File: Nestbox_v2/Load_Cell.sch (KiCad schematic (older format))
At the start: 30 parts

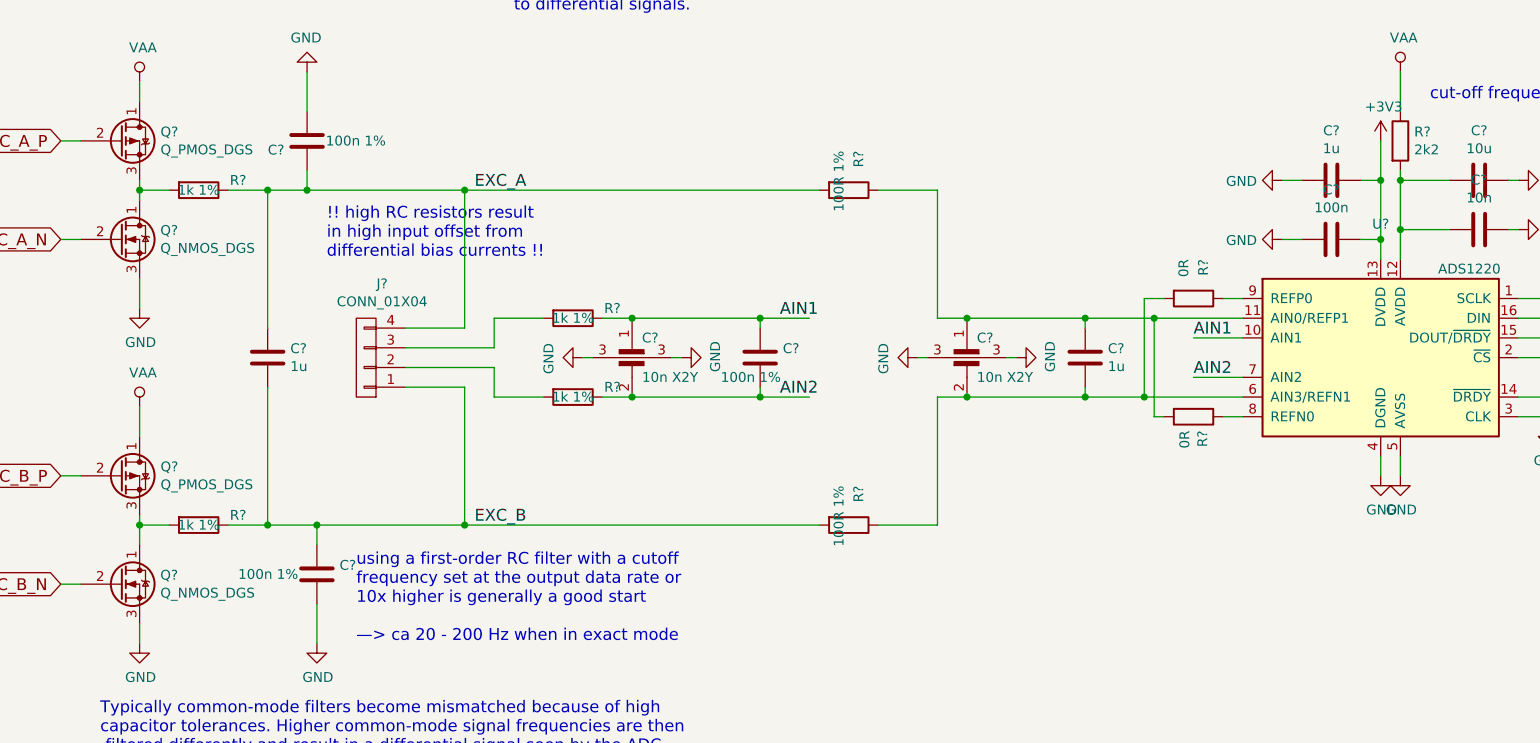
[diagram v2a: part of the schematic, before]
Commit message: created V2 MLX breakout board
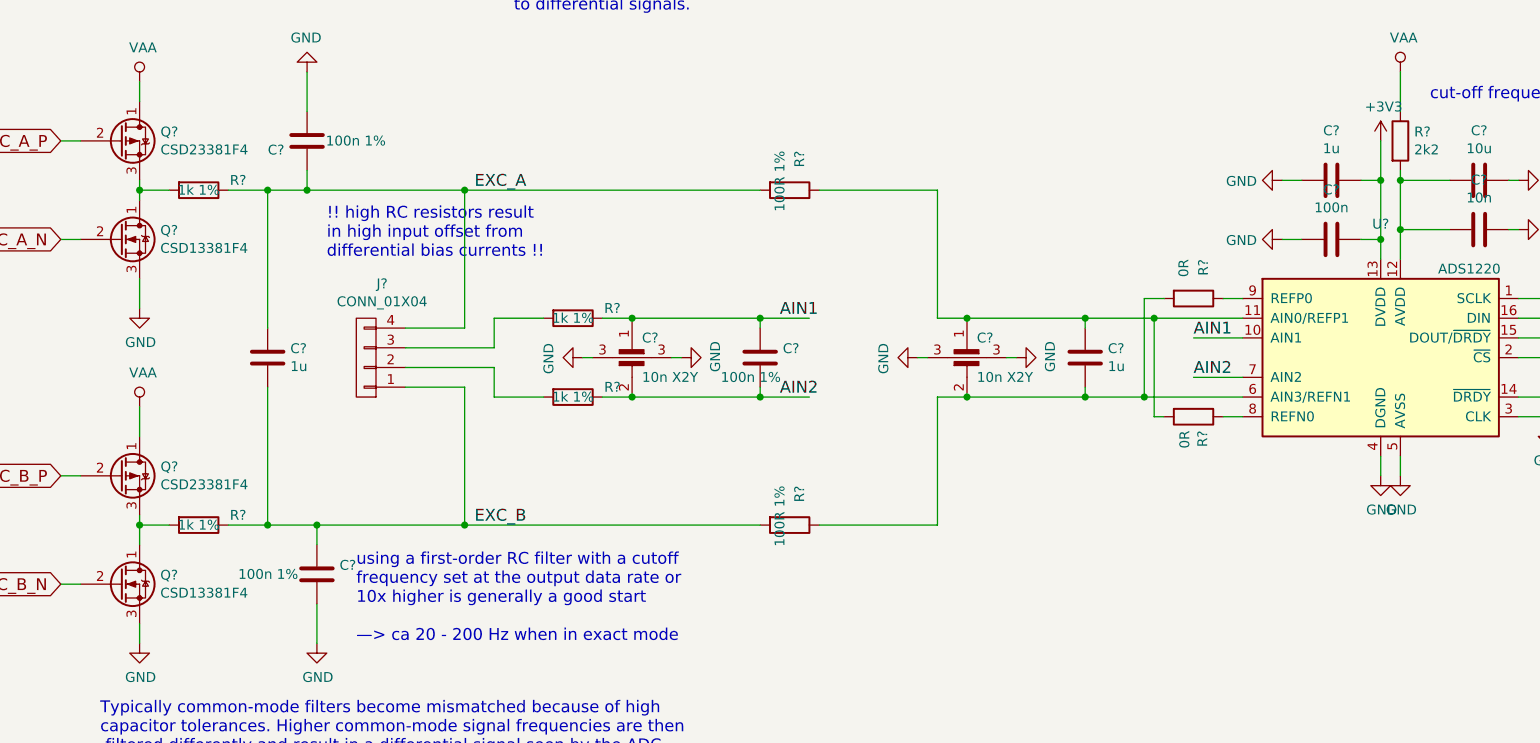
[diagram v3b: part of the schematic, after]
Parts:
- Q? (x2): value Q_NMOS_DGS -> CSD13381F4
- Q? (x2): value Q_PMOS_DGS -> CSD23381F4
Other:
- moved on the sheet: R?
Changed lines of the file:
@@
 P 1550 3400
 F 0 "Q?" H 1755 3446 50  0000 L CNN
-F 1 "Q_NMOS_DGS" H 1755 3355 50  0000 L CNN
+F 1 "CSD13381F4" H 1755 3355 50  0000 L CNN
 F 2 "" H 1750 3500 50  0001 C CNN
 F 3 "" H 1550 3400 50  0001 C CNN
@@
 P 1550 5150
 F 0 "Q?" H 1755 5196 50  0000 L CNN
-F 1 "Q_NMOS_DGS" H 1755 5105 50  0000 L CNN
+F 1 "CSD13381F4" H 1755 5105 50  0000 L CNN
 F 2 "" H 1750 5250 50  0001 C CNN
 F 3 "" H 1550 5150 50  0001 C CNN
@@
 P 1550 4600
 F 0 "Q?" H 1756 4646 50  0000 L CNN
-F 1 "Q_PMOS_DGS" H 1756 4555 50  0000 L CNN
+F 1 "CSD23381F4" H 1756 4555 50  0000 L CNN
 F 2 "" H 1750 4700 50  0001 C CNN
 F 3 "" H 1550 4600 50  0001 C CNN
@@
 P 1550 2900
 F 0 "Q?" H 1756 2946 50  0000 L CNN
-F 1 "Q_PMOS_DGS" H 1756 2855 50  0000 L CNN
+F 1 "CSD23381F4" H 1756 2855 50  0000 L CNN
 F 2 "" H 1750 3000 50  0001 C CNN
 F 3 "" H 1550 2900 50  0001 C CNN
@@
 L R R?
 U 1 1 5AF983FB
-P 5250 3150
-F 0 "R?" H 5050 3200 50  0000 L CNN
-F 1 "100R 1%" H 5050 3100 50  0000 L CNN
-F 2 "" V 5180 3150 50  0001 C CNN
-F 3 "" H 5250 3150 50  0001 C CNN
-	1    5250 3150
+P 4950 3150
+F 0 "R?" H 4750 3200 50  0000 L CNN
+F 1 "100R 1%" H 4750 3100 50  0000 L CNN
+F 2 "" V 4880 3150 50  0001 C CNN
+F 3 "" H 4950 3150 50  0001 C CNN
+	1    4950 3150
 	0    1    1    0
 $EndComp
@@
 L R R?
 U 1 1 5AF9851F
-P 5250 4850
-F 0 "R?" H 5050 4900 50  0000 L CNN
-F 1 "100R 1%" H 5050 4800 50  0000 L CNN
-F 2 "" V 5180 4850 50  0001 C CNN
-F 3 "" H 5250 4850 50  0001 C CNN
-	1    5250 4850
+P 4950 4850
+F 0 "R?" H 4750 4900 50  0000 L CNN
+F 1 "100R 1%" H 4750 4800 50  0000 L CNN
+F 2 "" V 4880 4850 50  0001 C CNN
+F 3 "" H 4950 4850 50  0001 C CNN
+	1    4950 4850
 	0    1    1    0
 $EndComp
@@
 EXC_B_N
 Wire Wire Line
-	8050 3050 8050 3500
+	8050 3050 8050 3100
+Wire Wire Line
+	8050 3100 8050 3350
+Wire Wire Line
+	8050 3350 8050 3500
 Wire Wire Line
 	8050 3100 8300 3100
 Connection ~ 8050 3100
 Wire Wire Line
-	7950 2900 7950 3500
+	7950 2900 7950 3100
+Wire Wire Line
+	7950 3100 7950 3400
+Wire Wire Line
+	7950 3400 7950 3500
 Wire Wire Line
 	8050 4600 8050 4500
@@
 	9050 3700 8650 3700
 Wire Wire Line
-	4000 3800 5050 3800
-Wire Wire Line
-	4000 4200 5050 4200
+	4000 3800 4150 3800
+Wire Wire Line
+	4150 3800 4800 3800
+Wire Wire Line
+	4800 3800 5050 3800
+Wire Wire Line
+	4000 4200 4150 4200
+Wire Wire Line
+	4150 4200 4800 4200
+Wire Wire Line
+	4800 4200 5050 4200
 Wire Wire Line
 	3700 3800 3450 3800
@@
 	3700 4200 3450 4200
 Wire Wire Line
-	5700 3800 7250 3800
-Wire Wire Line
-	5700 4200 7250 4200
+	5700 3800 5850 3800
+Wire Wire Line
+	5850 3800 6450 3800
+Wire Wire Line
+	6450 3800 6800 3800
+Wire Wire Line
+	6800 3800 7250 3800
+Wire Wire Line
+	5700 4200 5850 4200
+Wire Wire Line
+	5850 4200 6450 4200
+Wire Wire Line
+	6450 4200 6750 4200
+Wire Wire Line
+	6750 4200 7250 4200
 Wire Wire Line
 	6450 4200 6450 4150
 Wire Wire Line
-	2100 4850 5100 4850
+	2100 4850 2300 4850
+Wire Wire Line
+	2300 4850 2550 4850
+Wire Wire Line
+	2550 4850 3300 4850
+Wire Wire Line
+	3300 4850 4800 4850
 Connection ~ 6450 4200
 Wire Wire Line
@@
 	3300 3150 3300 3850
 Wire Wire Line
-	2100 3150 5100 3150
+	2100 3150 2300 3150
+Wire Wire Line
+	2300 3150 2500 3150
+Wire Wire Line
+	2500 3150 3300 3150
+Wire Wire Line
+	3300 3150 4800 3150
 Wire Wire Line
 	8050 2550 8050 2750
@@
 	1650 2600 1650 2700
 Wire Wire Line
-	1650 3100 1650 3200
+	1650 3100 1650 3150
+Wire Wire Line
+	1650 3150 1650 3200
 Connection ~ 3300 3150
 Connection ~ 1650 3150
 Wire Wire Line
-	1650 4800 1650 4950
+	1650 4800 1650 4850
+Wire Wire Line
+	1650 4850 1650 4950
 Connection ~ 3300 4850
 Connection ~ 1650 4850
@@
 	7250 4100 7000 4100
 Wire Wire Line
-	5400 3150 5700 3150
+	5100 3150 5700 3150
 Wire Wire Line
 	5700 3150 5700 3800
@@
 	5700 4200 5700 4850
 Wire Wire Line
-	5700 4850 5400 4850
+	5700 4850 5100 4850
 Connection ~ 5850 4200
 Wire Wire Line

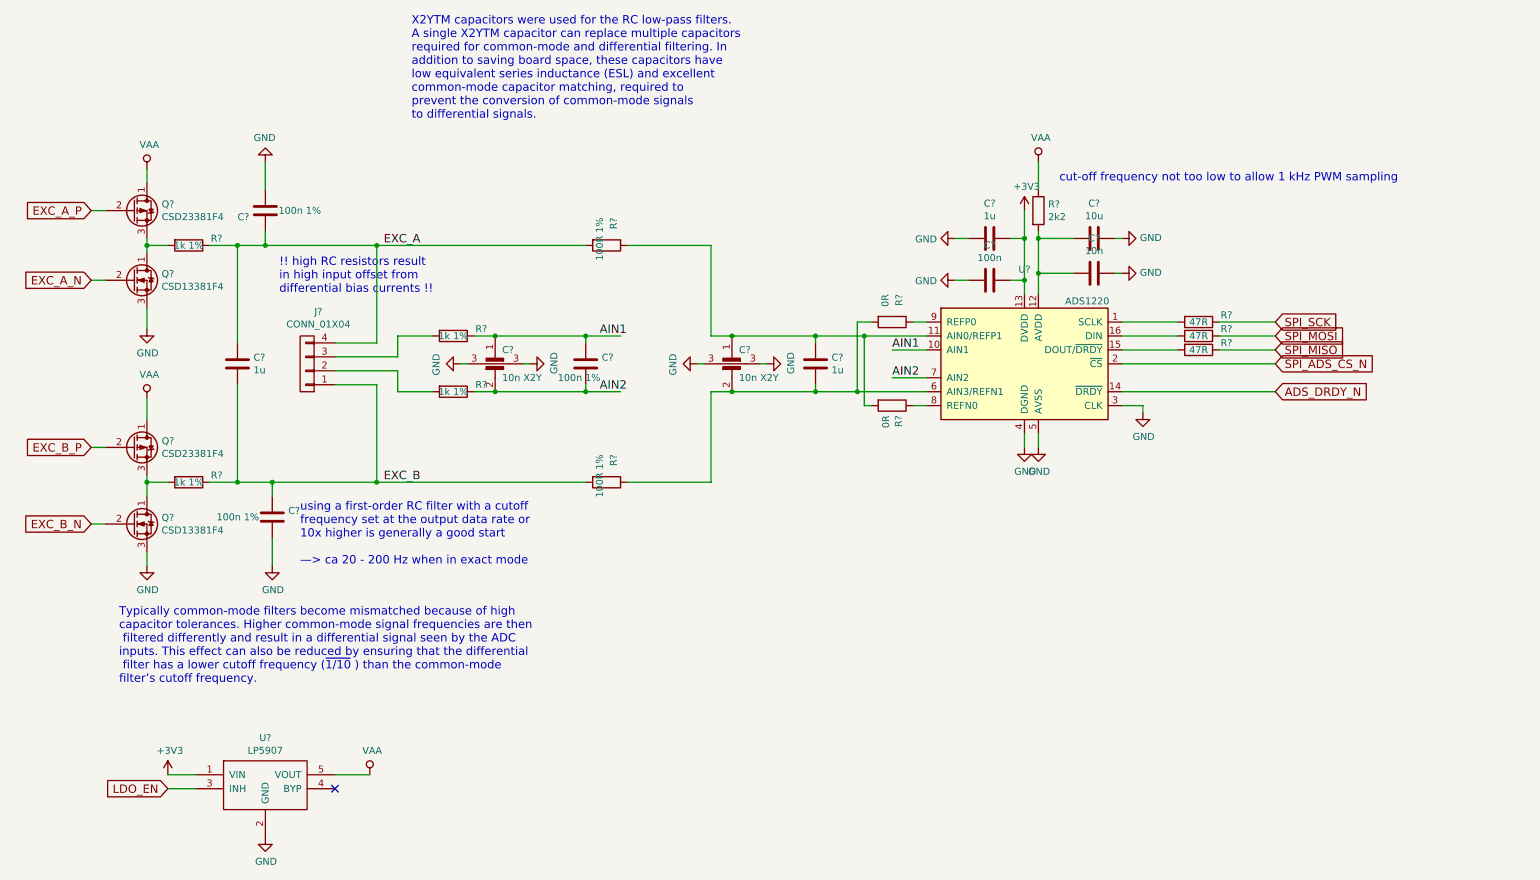
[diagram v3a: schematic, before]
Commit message: restructured top level sheet with hierarchical labels, assigned most GPIOs
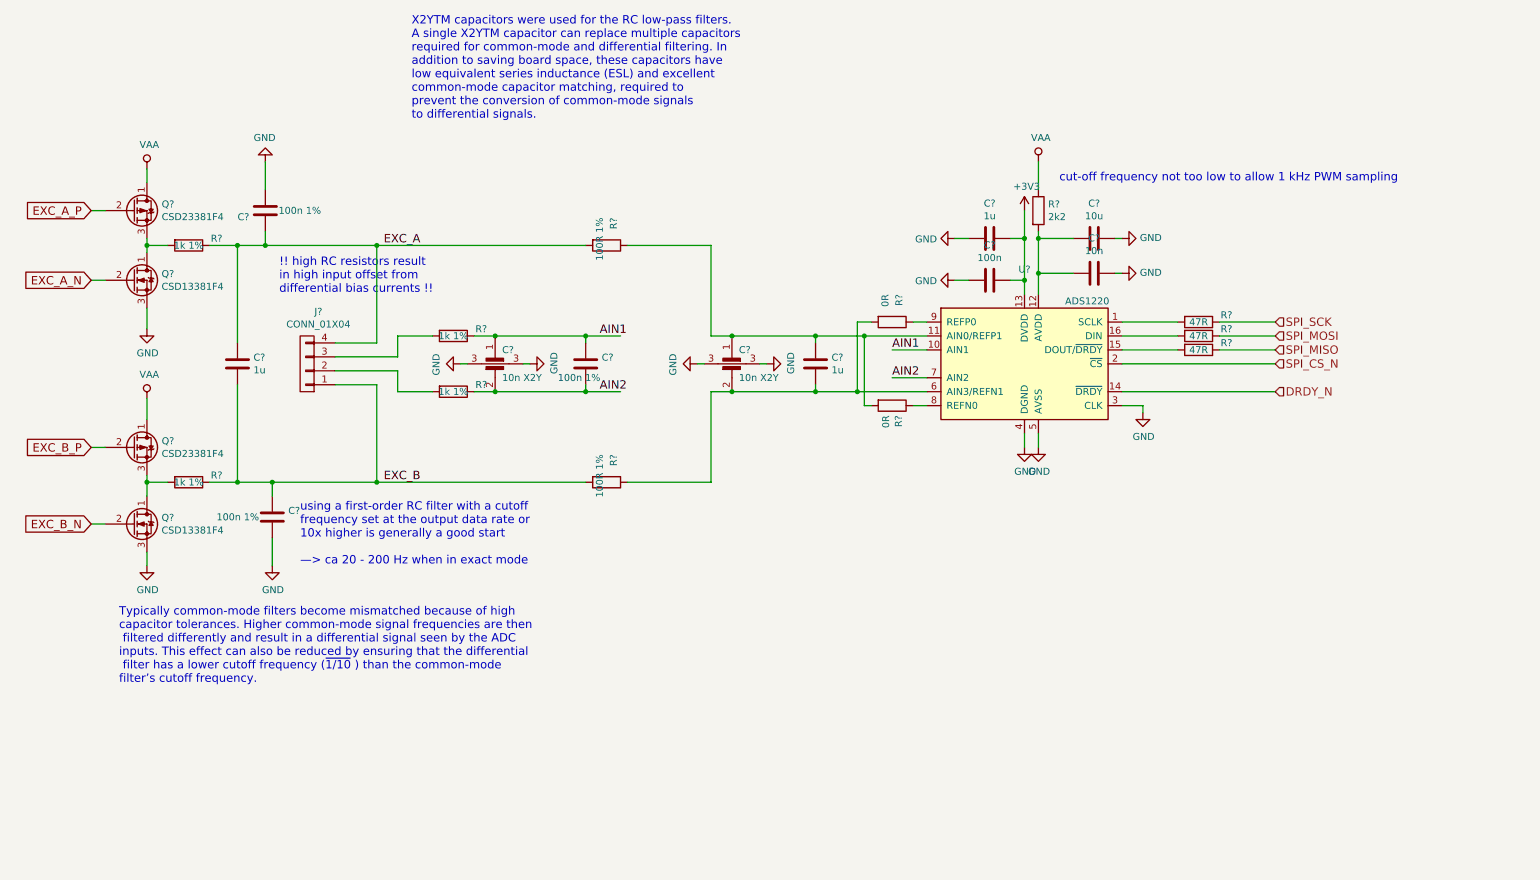
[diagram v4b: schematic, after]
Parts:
- removed U?: LP5907, TO_SOT_Packages_SMD:SOT-23-5, symbol LD3985M
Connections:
- net ADS_DRDY_N renamed DRDY_N
- net SPI_ADS_CS_N renamed SPI_CS_N
- no-connect marks 1 -> 0
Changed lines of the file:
@@
 LIBS:SeeedOPL-Transistor-2016
 LIBS:Nestbox_v2-cache
-EELAYER 26 0
+EELAYER 25 0
 EELAYER END
 $Descr A4 11693 8268
@@
 Text Notes 8200 2700 0    60   ~ 0
 cut-off frequency not too low to allow 1 kHz PWM sampling\n
-Text GLabel 9750 3700 2    60   Input ~ 0
-SPI_SCK
-Text GLabel 9750 3800 2    60   Input ~ 0
-SPI_MOSI
-Text GLabel 9750 3900 2    60   Input ~ 0
-SPI_MISO
-Text GLabel 9750 4000 2    60   Input ~ 0
-SPI_ADS_CS_N
 $Comp
 L C C?
@@
 	-1   0    0    1
 $EndComp
-Text GLabel 9750 4200 2    60   Input ~ 0
-ADS_DRDY_N
 $Comp
 L R R?
@@
 $EndComp
 $Comp
-L LD3985M U?
-U 1 1 5AF89C2B
-P 2500 7000
-F 0 "U?" H 2500 7315 50  0000 C CNN
-F 1 "LP5907" H 2500 7224 50  0000 C CNN
-F 2 "TO_SOT_Packages_SMD:SOT-23-5" H 2400 6750 50  0001 C CNN
-F 3 "" H 2500 7000 50  0001 C CNN
-	1    2500 7000
-	1    0    0    -1
-$EndComp
-$Comp
-L +3V3 #PWR?
-U 1 1 5AF8A704
-P 1800 6950
-F 0 "#PWR?" H 1800 6800 50  0001 C CNN
-F 1 "+3V3" H 1815 7123 50  0000 C CNN
-F 2 "" H 1800 6950 50  0001 C CNN
-F 3 "" H 1800 6950 50  0001 C CNN
-	1    1800 6950
-	1    0    0    -1
-$EndComp
-Text GLabel 1800 7050 0    60   Input ~ 0
-LDO_EN
-$Comp
-L GND #PWR?
-U 1 1 5AF8A996
-P 2500 7400
-F 0 "#PWR?" H 2500 7150 50  0001 C CNN
-F 1 "GND" H 2505 7227 50  0000 C CNN
-F 2 "" H 2500 7400 50  0001 C CNN
-F 3 "" H 2500 7400 50  0001 C CNN
-	1    2500 7400
-	1    0    0    -1
-$EndComp
-NoConn ~ 3000 7050
-$Comp
 L GND #PWR?
 U 1 1 5AF8B9E6
@@
 F 3 "" H 1650 5450 50  0001 C CNN
 	1    1650 5450
-	1    0    0    -1
-$EndComp
-$Comp
-L VAA #PWR?
-U 1 1 5AF8BE4C
-P 3250 6950
-F 0 "#PWR?" H 3250 6800 50  0001 C CNN
-F 1 "VAA" H 3267 7123 50  0000 C CNN
-F 2 "" H 3250 6950 50  0001 C CNN
-F 3 "" H 3250 6950 50  0001 C CNN
-	1    3250 6950
 	1    0    0    -1
 $EndComp
@@
 	8050 2550 8050 2750
 Wire Wire Line
-	1800 6950 2000 6950
-Wire Wire Line
-	2000 7050 1800 7050
-Wire Wire Line
-	3000 6950 3250 6950
-Wire Wire Line
 	1650 2600 1650 2700
 Wire Wire Line
@@
 Wire Wire Line
 	1250 5150 1350 5150
+Text HLabel 9750 3700 2    60   Input ~ 0
+SPI_SCK
+Text HLabel 9750 3800 2    60   Input ~ 0
+SPI_MOSI
+Text HLabel 9750 3900 2    60   Input ~ 0
+SPI_MISO
+Text HLabel 9750 4000 2    60   Input ~ 0
+SPI_CS_N
+Text HLabel 9750 4200 2    60   Input ~ 0
+DRDY_N
 $EndSCHEMATC

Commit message: finished power supply schematics
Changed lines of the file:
@@
 Text Label 4900 3800 0    60   ~ 0
 AIN1
-Text GLabel 1250 2900 0    60   Input ~ 0
-EXC_A_P
-Text GLabel 1250 3400 0    60   Input ~ 0
-EXC_A_N
-Text GLabel 1250 4600 0    60   Input ~ 0
-EXC_B_P
-Text GLabel 1250 5150 0    60   Input ~ 0
-EXC_B_N
 Wire Wire Line
 	8050 3050 8050 3100
@@
 Text HLabel 9750 4200 2    60   Input ~ 0
 DRDY_N
+Text HLabel 1250 2900 0    60   Input ~ 0
+EXC_A_P
+Text HLabel 1250 3400 0    60   Input ~ 0
+EXC_A_N
+Text HLabel 1250 5150 0    60   Input ~ 0
+EXC_B_N
+Text HLabel 1250 4600 0    60   Input ~ 0
+EXC_B_P
 $EndSCHEMATC
